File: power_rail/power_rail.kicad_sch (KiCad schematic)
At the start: 14 parts, among them J1 Conn_01x06, J2 Conn_02x08_Row_Letter_Last, J3 Conn_02x08_Row_Letter_Last, J4 Conn_02x08_Row_Letter_Last, J5 Conn_02x08_Row_Letter_Last, J6 Conn_02x08_Row_Letter_Last, J7 Conn_02x08_Row_Letter_Last, J8 Conn_01x06

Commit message: VCA v. 2.0
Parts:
- removed J1, J8: Conn_01x06, Connector_Wire:SolderWire-0.75sqmm_1x06_P4.8mm_D1.25mm_OD2.3mm, symbol Connector_Generic:Conn_01x06
- added J1, J11, J12, J13, J14, J15, J16, J17, J18, J19, J20, J8: Conn_01x01_Pin, power_rail_elements:Blade_3866B.68, symbol Connector:Conn_01x01_Pin
- added J9: Conn_02x08_Row_Letter_Last, Connector_IDC:IDC-Header_2x08_P2.54mm_Vertical, symbol Connector_Generic:Conn_02x08_Odd_Even
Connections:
- net +12V: now also J13.1 (Pin_1), J18.1 (Pin_1), J9.10 (Pin_10), J9.9 (Pin_9)
- net +5V: now also J12.1 (Pin_1), J17.1 (Pin_1), J9.11 (Pin_11), J9.12 (Pin_12)
- net -12V: now also J15.1 (Pin_1), J20.1 (Pin_1), J9.1 (Pin_1), J9.2 (Pin_2)
- net CV: now also J11.1 (Pin_1), J16.1 (Pin_1), J9.13 (Pin_13), J9.14 (Pin_14)
- net GND: now also J14.1 (Pin_1), J19.1 (Pin_1), J9.3 (Pin_3), J9.4 (Pin_4), J9.5 (Pin_5), J9.6 (Pin_6), J9.7 (Pin_7), J9.8 (Pin_8)
- net Gate: now also J1.1 (Pin_1), J8.1 (Pin_1), J9.15 (Pin_15), J9.16 (Pin_16)

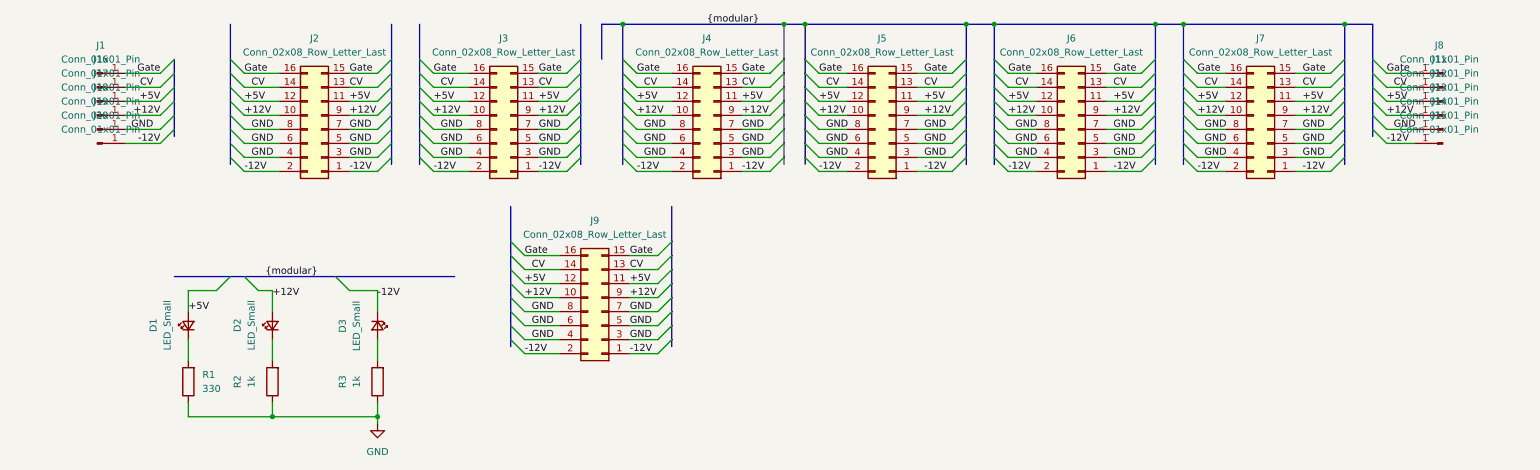
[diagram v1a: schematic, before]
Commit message: Simulated exponential VCA control stage
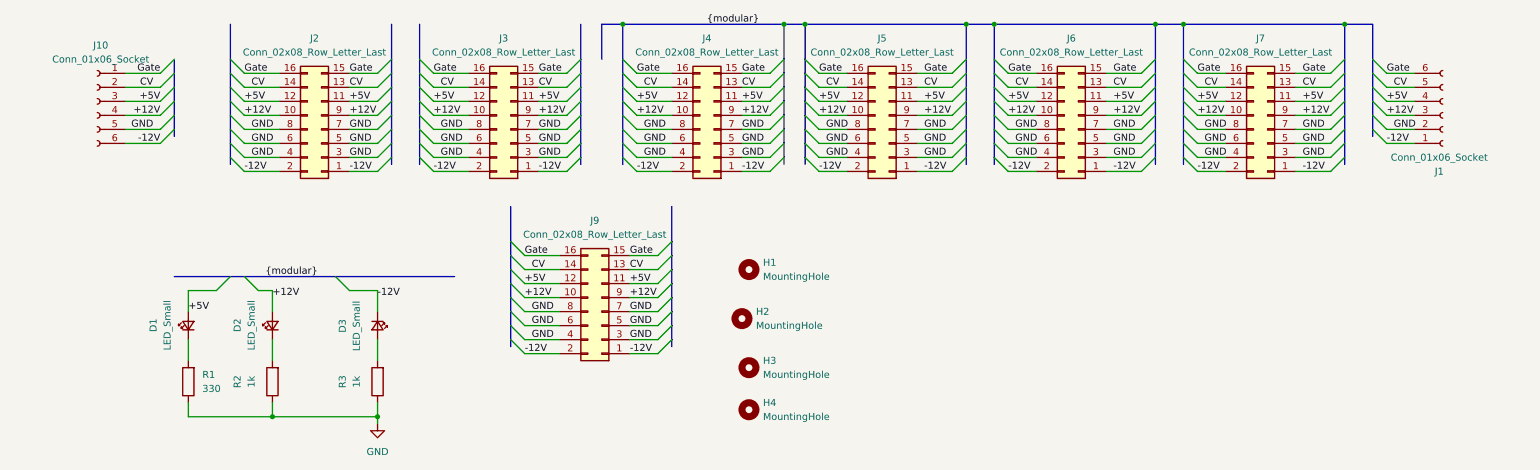
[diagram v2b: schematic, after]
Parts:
- removed J1, J11, J12, J13, J14, J15, J16, J17, J18, J19, J20, J8: Conn_01x01_Pin, power_rail_elements:Blade_3866B.68, symbol Connector:Conn_01x01_Pin
- added H1, H2, H3, H4: MountingHole, MountingHole:MountingHole_3.2mm_M3, symbol Mechanical:MountingHole
- added J1, J10: Conn_01x06_Socket, TerminalBlock_Phoenix:TerminalBlock_Phoenix_MKDS-1,5-6-5.08_1x06_P5.08mm_Horizontal, symbol Connector:Conn_01x06_Socket
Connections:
- net +12V: now also J1.3 (Pin_3), J10.4 (Pin_4)
- net +5V: now also J1.4 (Pin_4), J10.3 (Pin_3)
- net -12V: now also J1.1 (Pin_1), J10.6 (Pin_6)
- net CV: now also J1.5 (Pin_5), J10.2 (Pin_2)
- net GND: now also J1.2 (Pin_2), J10.5 (Pin_5)
- net Gate: now also J1.6 (Pin_6), J10.1 (Pin_1)

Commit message: Exponential VCA ver. 1.2
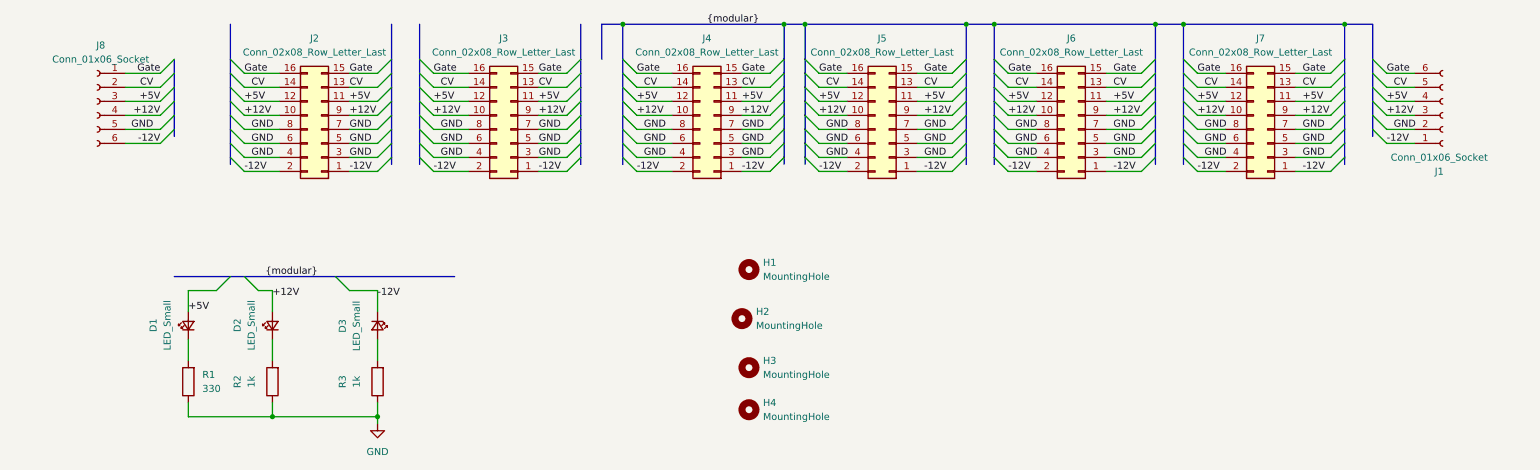
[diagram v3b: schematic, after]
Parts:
- removed J9: Conn_02x08_Row_Letter_Last, Connector_IDC:IDC-Header_2x08_P2.54mm_Vertical, symbol Connector_Generic:Conn_02x08_Odd_Even
- J1: footprint TerminalBlock_Phoenix:TerminalBlock_Phoenix_MKDS-1,5-6-5.08_1x06_P5.08mm_Horizontal -> power_rail_elements:TerminalBlock_Phoenix_MKDS-1,5-6-5.08_1x06_P5.08mm_Horizontal
- J8: renamed from J10; footprint TerminalBlock_Phoenix:TerminalBlock_Phoenix_MKDS-1,5-6-5.08_1x06_P5.08mm_Horizontal -> power_rail_elements:TerminalBlock_Phoenix_MKDS-1,5-6-5.08_1x06_P5.08mm_Horizontal
